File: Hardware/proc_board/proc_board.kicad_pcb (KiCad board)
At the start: 2 copper layers, 80.8 x 60.1 mm, 17 parts, among them J1 Conn_01x40, U1 GAL16V8, U2 W65C02SxP, U3 HM62256BLP, U4 28C256

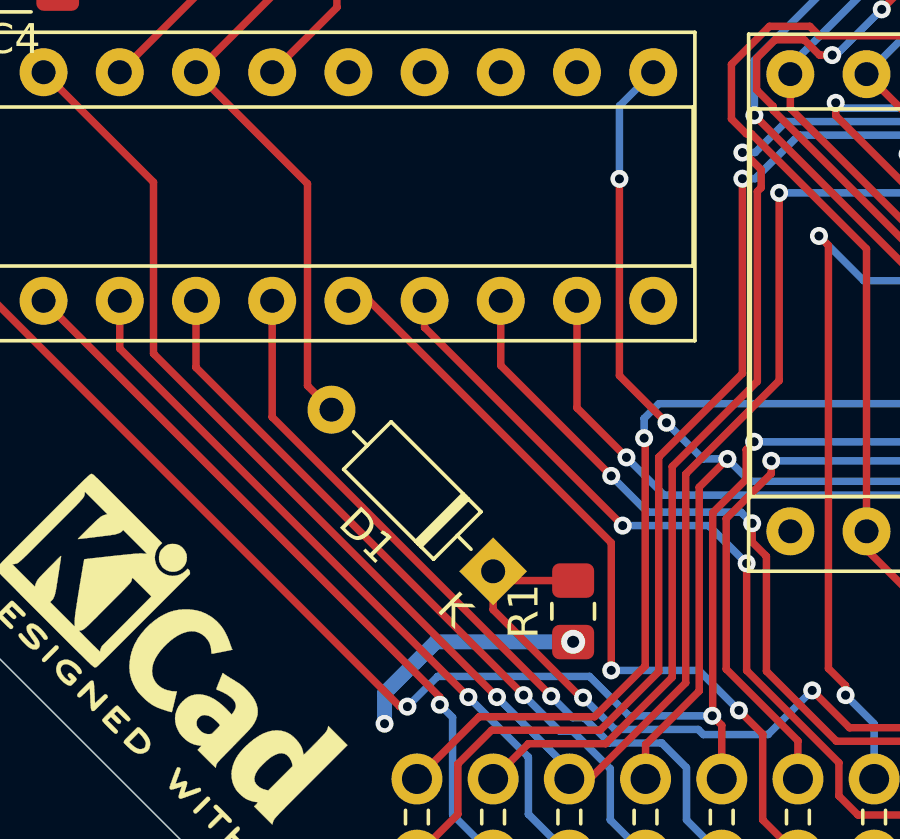
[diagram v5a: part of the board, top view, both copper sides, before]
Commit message: Backplane provides diode and pullups for SLOW signal
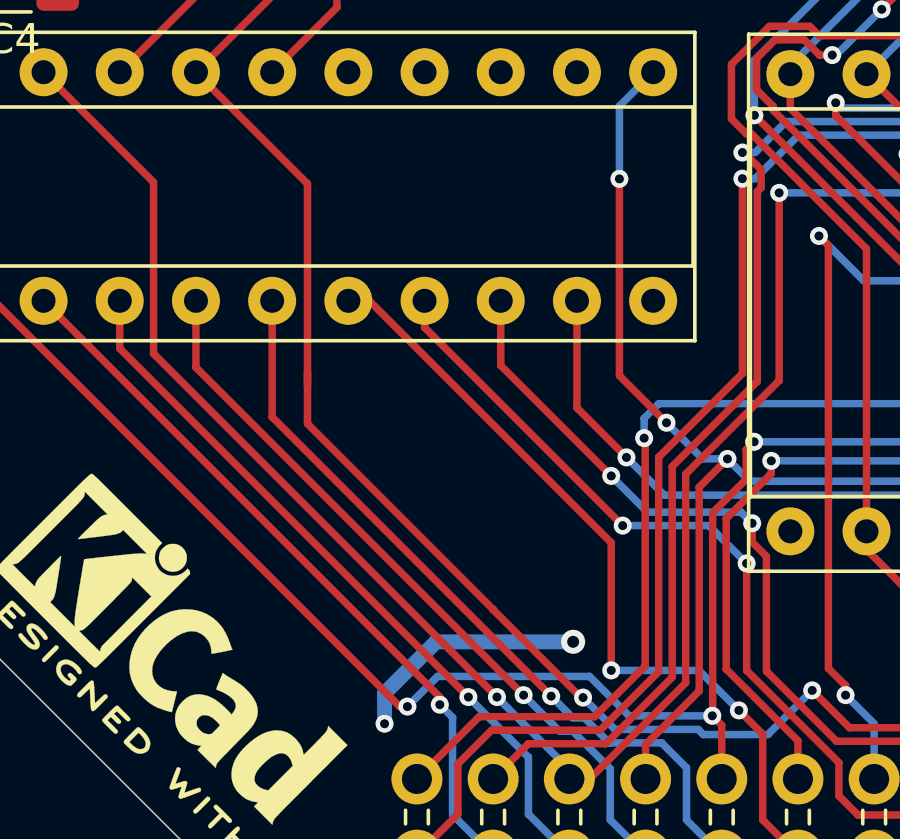
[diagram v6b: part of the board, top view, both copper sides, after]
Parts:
- removed D1: 1N4148, Diode_THT:D_DO-35_SOD27_P7.62mm_Horizontal
- removed R1: 4.7k, Resistor_SMD:R_0805_2012Metric_Pad1.15x1.40mm_HandSolder
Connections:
- J1 pad 22: ~SLOW~ -> ~ROM_CS~
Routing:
- net ~ROM_CS~: track 44.1 -> 92.3 mm, vias 3 -> 6
- net ~SLOW~: track 43.0 -> 0.00 mm, vias 3 -> 0
